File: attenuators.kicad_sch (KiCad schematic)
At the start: 16 parts, among them K301 FTR-B3GA4.5Z-B10, K302 FTR-B3GA4.5Z-B10, Q301 BC817, Q302 BC817

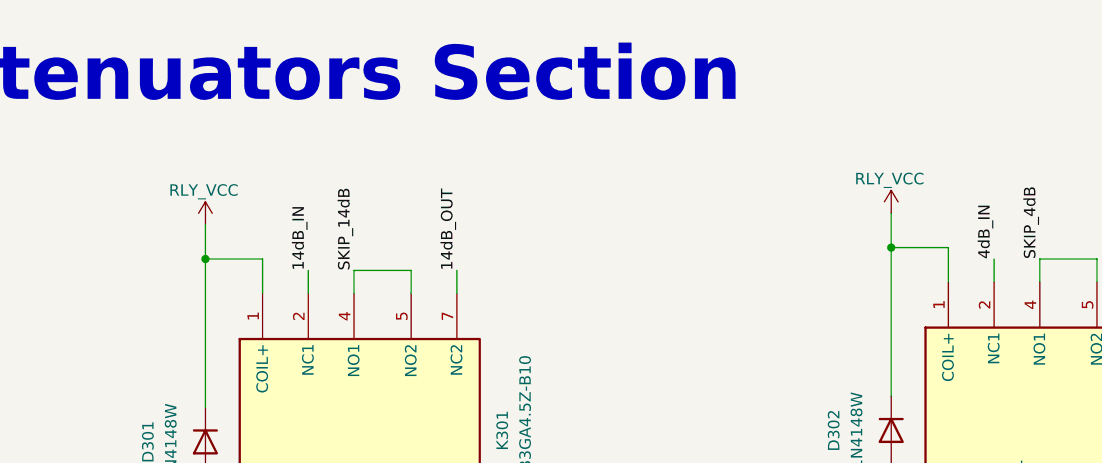
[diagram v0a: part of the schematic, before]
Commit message: finished individual block placement and started integrating, might need to change the AFEs length
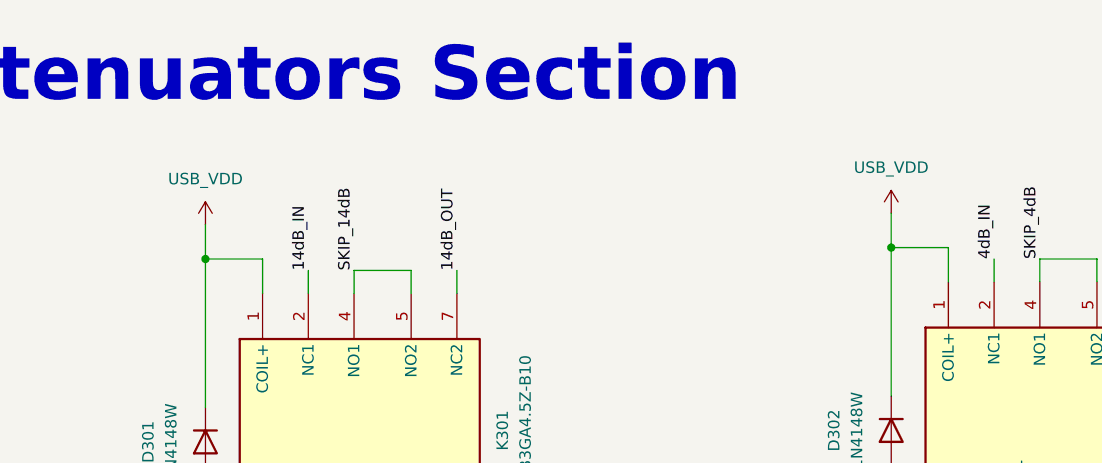
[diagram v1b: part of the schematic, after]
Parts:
- C701, C703: footprint (none) -> Capacitor_SMD:C_0603_1608Metric; MPN (none) -> FCC0603N100J500CT
- C702: footprint (none) -> Capacitor_SMD:C_0603_1608Metric; MPN (none) -> CC0603JRNPO9BN510
- C704: footprint (none) -> Capacitor_SMD:C_0603_1608Metric; MPN (none) -> 0603N180J500CT
- D301, D302: MPN (none) -> 1N4148W
- K301, K302: footprint FTRB3GA45ZB10 -> FTR-B3GA4.5Z-B10:FTRB3GA45ZB10; MPN (none) -> FTR-B3GA4.5Z-B10
- Q301, Q302: MPN (none) -> BC817
- R301, R309: footprint (none) -> Resistor_SMD:R_0603_1608Metric; MPN (none) -> RT0603BRD07500RL
- R302: footprint (none) -> Resistor_SMD:R_0603_1608Metric; MPN (none) -> HoARG0603-1/10W-820KR-0.1%-TCR25
- R303: footprint (none) -> Resistor_SMD:R_0603_1608Metric; MPN (none) -> ERA3AEB204V
- R304: footprint (none) -> Resistor_SMD:R_0603_1608Metric; MPN (none) -> ARG03BTC3653
- R305: footprint (none) -> Resistor_SMD:R_0603_1608Metric; MPN (none) -> ARG03BTC6493
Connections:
- net RLY_VCC renamed USB_VDD
